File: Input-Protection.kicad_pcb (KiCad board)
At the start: 2 copper layers, 80 x 40 mm, 58 parts, among them J101 KLDX-0202-B, J102 EBWA-02-B, J103 EBWA-02-B, J104 KLDX-0202-B, Q201 MCU18P10Y-TP, Q601 BC846, Q602 MCU18P10Y-TP, U401 LM4040N-5.0, U501 AZV3002S-13

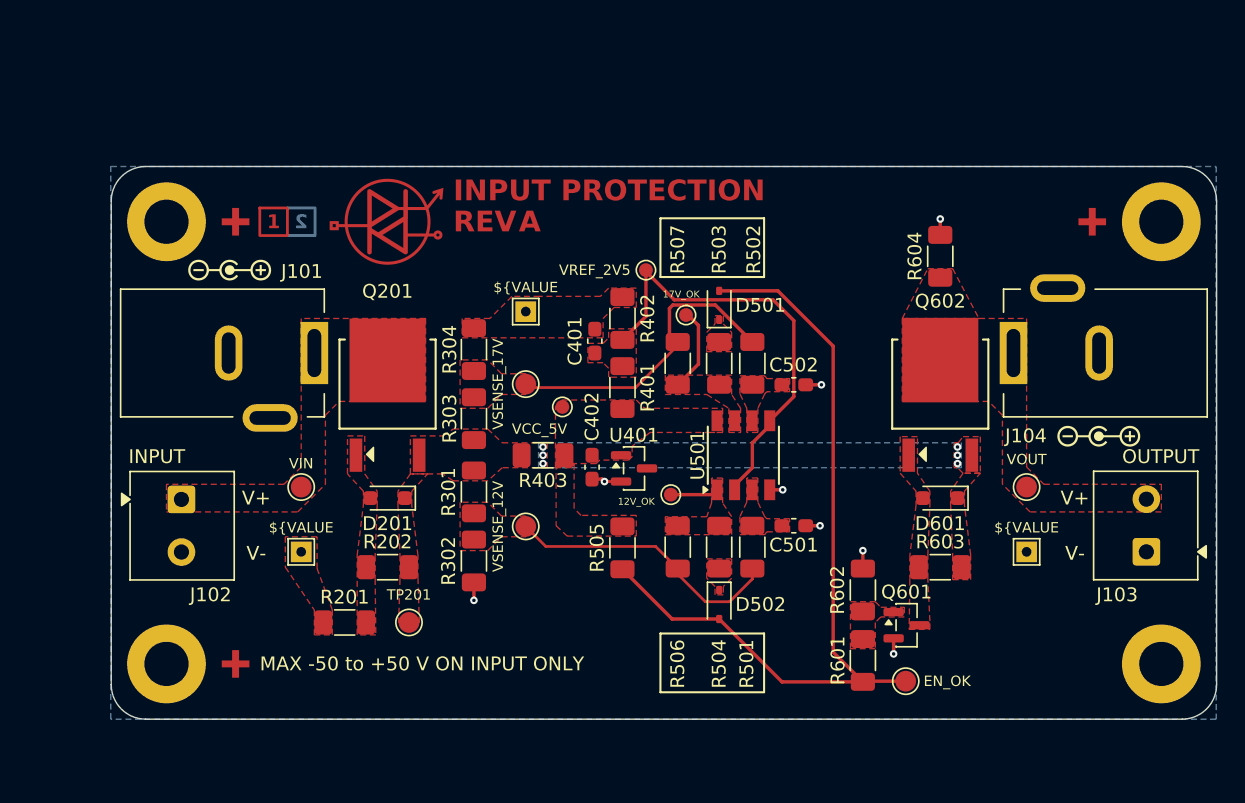
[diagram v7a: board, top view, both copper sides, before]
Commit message: feat!: added OC protection, redesigned board from near scratch, size increase
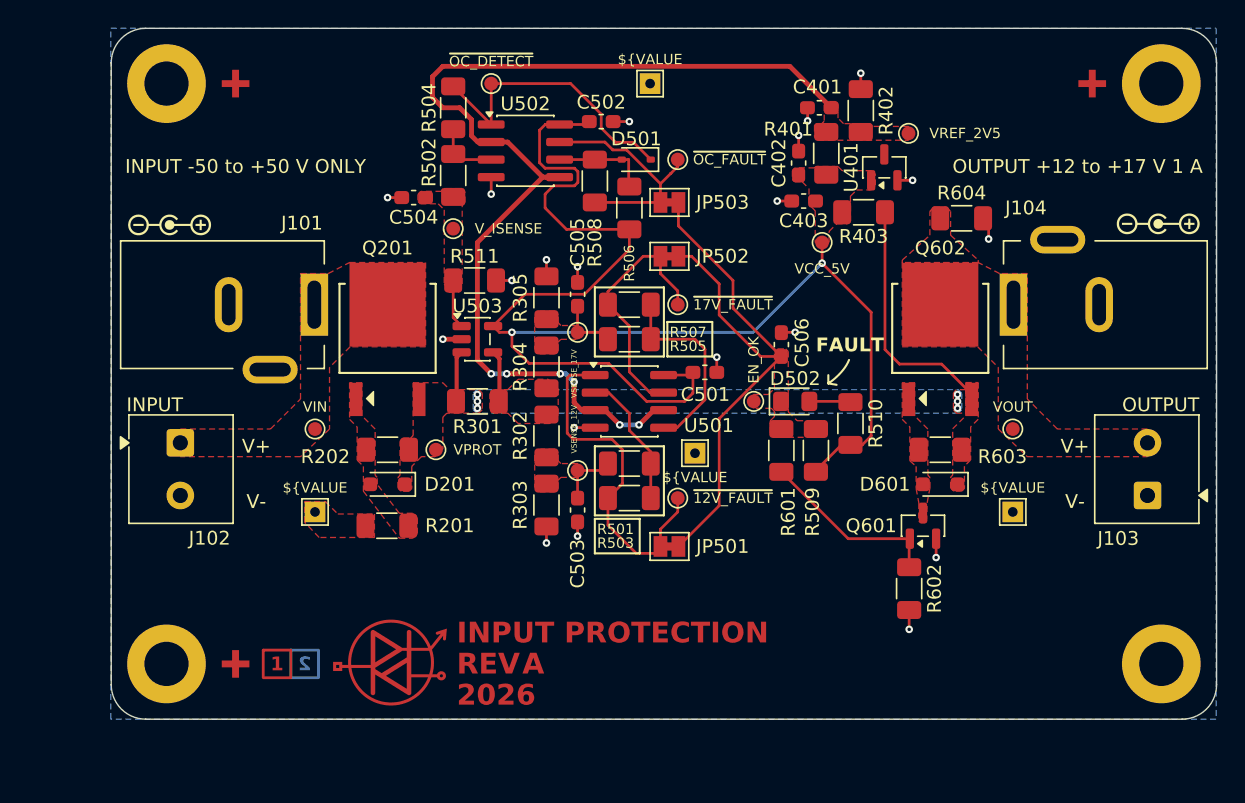
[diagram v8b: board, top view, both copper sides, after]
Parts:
- removed TP403: VCC_5V, RD-Testpoints:TestPoint_Pad_D1.0mm
- added C403: 100n, Capacitor_SMD:C_0603_1608Metric_Pad1.08x0.95mm_HandSolder, F.Cu at (167.7, 64.2)
- added C503: 10n, Capacitor_SMD:C_0603_1608Metric_Pad1.08x0.95mm_HandSolder, F.Cu at (151.3, 86.5)
- added C504: 10n, Capacitor_SMD:C_0603_1608Metric_Pad1.08x0.95mm_HandSolder, F.Cu at (139.5, 63.9)
- added C505: 10n, Capacitor_SMD:C_0603_1608Metric_Pad1.08x0.95mm_HandSolder, F.Cu at (151.3, 70.9)
- added C506: 1u, Capacitor_SMD:C_0603_1608Metric_Pad1.08x0.95mm_HandSolder, F.Cu at (166.1, 74.5)
- added JP501: SolderJumper_2_Bridged, Jumper:SolderJumper-2_P1.3mm_Bridged_Pad1.0x1.5mm, F.Cu at (158.0, 89.2)
- added JP502: SolderJumper_2_Bridged, Jumper:SolderJumper-2_P1.3mm_Bridged_Pad1.0x1.5mm, F.Cu at (158.0, 68.2)
- added JP503: SolderJumper_2_Bridged, Jumper:SolderJumper-2_P1.3mm_Bridged_Pad1.0x1.5mm, F.Cu at (158.0, 64.2)
- added R305: 10k, Resistor_SMD:R_1206_3216Metric_Pad1.30x1.75mm_HandSolder, F.Cu at (149.1, 71.2)
- added R508: 10k, Resistor_SMD:R_1206_3216Metric_Pad1.30x1.75mm_HandSolder, F.Cu at (152.6, 62.7)
- added R509: 10k, Resistor_SMD:R_1206_3216Metric_Pad1.30x1.75mm_HandSolder, F.Cu at (168.6, 82.2)
- added R510: 3.32k, Resistor_SMD:R_1206_3216Metric_Pad1.30x1.75mm_HandSolder, F.Cu at (171.1, 80.3)
- added R511: 22.1k, Resistor_SMD:R_1206_3216Metric_Pad1.30x1.75mm_HandSolder, F.Cu at (143.9, 69.9)
- added TP402: VCC_5V, RD-Testpoints:TestPoint_Pad_D1.0mm, F.Cu at (169.0, 67.2)
- added TP504: ~{OC_FAULT}, RD-Testpoints:TestPoint_Pad_D1.0mm, F.Cu at (158.6, 61.1)
- added TP505: V_ISENSE, RD-Testpoints:TestPoint_Pad_D1.0mm, F.Cu at (142.3, 66.2)
- added TP506: EN_OK, RD-Testpoints:TestPoint_Pad_D1.0mm, F.Cu at (164.1, 78.7)
- added TP507: GND, RD-Testpoints:TestPoint_THTPad_1.5x1.5mm_Drill0.7mm, F.Cu at (156.6, 55.6)
- added U502: LM393, Package_SO:SOIC-8_3.9x4.9mm_P1.27mm, F.Cu at (147.5, 60.5)
- added U503: INA169NA/3K, Package_TO_SOT_SMD:SOT-23-5, F.Cu at (144.1, 74.2)
- C402: value 100n -> 1u
- C501, C502: value 10n -> 100n
- D502: value 1N4148WS -> LED; footprint Diode_SMD:D_SOD-323 -> LED_SMD:LED_0805_2012Metric_Pad1.15x1.40mm_HandSolder
- R301: value 39.2k -> 100m
- R302: value 10k -> 39.2k
- R303: value 56.2k -> 10k
- R304: value 10k -> 56.2k
- R403: value 10k -> 3.32k
- R503, R504: value 470 -> 1M
- R505: value 47k -> 1k
- R506: value 1M -> 100k
- TP102, TP103, TP201, TP302, TP303: footprint RD-Testpoints:TestPoint_Pad_D1.5mm -> RD-Testpoints:TestPoint_Pad_D1.0mm
- TP501: value 12V_OK -> ~{12V_FAULT}
- TP502: value 17V_OK -> ~{OC_DETECT}
- TP503: value EN_OK -> ~{17V_FAULT}; footprint RD-Testpoints:TestPoint_Pad_D1.5mm -> RD-Testpoints:TestPoint_Pad_D1.0mm
- U501: value AZV3002S-13 -> LM393; footprint AZV3002S-13:Diodes_SO-8EP -> Package_SO:SOIC-8_3.9x4.9mm_P1.27mm
- moved R504 37.2 mm to (142.3, 57.4)
- moved ID901 32.0 mm to (130.6, 97.7)
- moved TP503 31.9 mm to (158.6, 71.7)
- moved R403 29.1 mm to (172.0, 65.0), turned to 0 degrees
- moved U401 28.3 mm to (173.5, 61.7), turned to 90 degrees
- moved C402 26.6 mm to (167.3, 61.4), turned to 90 degrees
- moved R502 25.6 mm to (142.3, 62.3)
- moved R506 24.8 mm to (155.1, 64.7), turned to -90 degrees
- moved C502 23.6 mm to (153.0, 58.4)
- moved C401 23.4 mm to (168.8, 57.4), turned to 180 degrees
- moved R402 22.9 mm to (171.8, 57.6)
- moved R401 22.5 mm to (169.3, 60.7)
- moved TP502 21.9 mm to (145.1, 55.6)
- moved TP401 21.4 mm to (175.3, 59.2), turned to 90 degrees
- moved R601 16.3 mm to (166.1, 82.2), turned to 90 degrees
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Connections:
- C501 pad 1: Net-(U501A-+) -> VCC_5V
- C502 pad 1: Net-(U501B--) -> VCC_5V
- D501 pad 1: Net-(D501-K) -> /ARCHITECTURE/5. COMPARATOR/~{OC_DETECT}
- D501 pad 2: /ARCHITECTURE/5. COMPARATOR/EN_OK -> /ARCHITECTURE/5. COMPARATOR/LATCH_IN
- D502 pad 1: Net-(D502-K) -> /ARCHITECTURE/5. COMPARATOR/EN_OK
- D502 pad 2: /ARCHITECTURE/5. COMPARATOR/EN_OK -> Net-(D502-A)
- R301 pad 1: /ARCHITECTURE/3. SENSING/VSENSE_12V -> /ARCHITECTURE/3. SENSING/ISENSE_N
- R302 pad 1: GND -> /ARCHITECTURE/3. SENSING/VSENSE_12V
- R302 pad 2: /ARCHITECTURE/3. SENSING/VSENSE_12V -> /ARCHITECTURE/3. SENSING/ISENSE_N
- R303 pad 1: /ARCHITECTURE/3. SENSING/VSENSE_17V -> GND
- R303 pad 2: /ARCHITECTURE/2. POLARITY PROTECTION/VPROT -> /ARCHITECTURE/3. SENSING/VSENSE_12V
- R304 pad 1: GND -> /ARCHITECTURE/3. SENSING/VSENSE_17V
- R304 pad 2: /ARCHITECTURE/3. SENSING/VSENSE_17V -> /ARCHITECTURE/3. SENSING/ISENSE_N
- R501 pad 1: Net-(U501A-+) -> Net-(U501A--)
- R502 pad 1: Net-(U501B--) -> /ARCHITECTURE/5. COMPARATOR/V_ISENSE
- R502 pad 2: /ARCHITECTURE/3. SENSING/VSENSE_17V -> Net-(U502A-+)
- R503 pad 1: Net-(D501-K) -> Net-(U501A--)
- R503 pad 2: /ARCHITECTURE/5. COMPARATOR/17V_OK -> /ARCHITECTURE/5. COMPARATOR/~{12V_FAULT}
- R504 pad 1: Net-(D502-K) -> Net-(U502A-+)
- R504 pad 2: /ARCHITECTURE/5. COMPARATOR/12V_OK -> /ARCHITECTURE/5. COMPARATOR/~{OC_DETECT}
- R505 pad 1: /ARCHITECTURE/5. COMPARATOR/EN_OK -> /ARCHITECTURE/3. SENSING/VSENSE_17V
- R505 pad 2: VCC_5V -> Net-(U501B-+)
- R506 pad 1: /ARCHITECTURE/3. SENSING/VSENSE_12V -> /ARCHITECTURE/5. COMPARATOR/LATCH_IN
- R506 pad 2: /ARCHITECTURE/5. COMPARATOR/12V_OK -> VCC_5V
- R507 pad 1: /ARCHITECTURE/3. SENSING/VSENSE_17V -> Net-(U501B-+)
- R507 pad 2: /ARCHITECTURE/5. COMPARATOR/17V_OK -> /ARCHITECTURE/5. COMPARATOR/~{17V_FAULT}
- TP501 pad 1: /ARCHITECTURE/5. COMPARATOR/12V_OK -> /ARCHITECTURE/5. COMPARATOR/~{12V_FAULT}
- TP502 pad 1: /ARCHITECTURE/5. COMPARATOR/17V_OK -> /ARCHITECTURE/5. COMPARATOR/~{OC_DETECT}
- TP503 pad 1: /ARCHITECTURE/5. COMPARATOR/EN_OK -> /ARCHITECTURE/5. COMPARATOR/~{17V_FAULT}
- U501 pad 1: /ARCHITECTURE/5. COMPARATOR/12V_OK -> /ARCHITECTURE/5. COMPARATOR/~{12V_FAULT}
- U501 pad 2: VREF_2V5 -> Net-(U501A--)
- U501 pad 3: Net-(U501A-+) -> VREF_2V5
- U501 pad 5: VREF_2V5 -> Net-(U501B-+)
- U501 pad 6: Net-(U501B--) -> VREF_2V5
- U501 pad 7: /ARCHITECTURE/5. COMPARATOR/17V_OK -> /ARCHITECTURE/5. COMPARATOR/~{17V_FAULT}
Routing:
- net VCC_5V: track 0.00 -> 100.6 mm, vias 0 -> 2
- net VREF_2V5: track 31.8 -> 76.1 mm, vias 0 -> 6
- net /ARCHITECTURE/5. COMPARATOR/~{12V_FAULT}: track 0.00 -> 25.7 mm
- net /ARCHITECTURE/2. POLARITY PROTECTION/VPROT: track 0.00 -> 21.6 mm
- net /ARCHITECTURE/5. COMPARATOR/~{OC_DETECT}: track 0.00 -> 21.3 mm
- net /ARCHITECTURE/5. COMPARATOR/~{17V_FAULT}: track 0.00 -> 18.4 mm
- net /ARCHITECTURE/3. SENSING/VSENSE_17V: track 22.6 -> 4.29 mm
- net /ARCHITECTURE/5. COMPARATOR/~{OC_FAULT}: track 0.00 -> 17.1 mm
- net /ARCHITECTURE/5. COMPARATOR/EN_OK: track 59.5 -> 42.9 mm
- net /ARCHITECTURE/3. SENSING/VSENSE_12V: track 20.3 -> 4.41 mm
- net Net-(U501B-+): track 0.00 -> 14.2 mm
- net GND: track 10.2 -> 24.0 mm, vias 8 -> 20
- net Net-(Q601-B): track 0.00 -> 13.4 mm
- net Net-(U501A--): track 0.00 -> 10.1 mm
- net /ARCHITECTURE/5. COMPARATOR/LATCH_IN: track 0.00 -> 6.47 mm
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- added copper zone on F.Cu, net /ARCHITECTURE/3. SENSING/ISENSE_N
- added copper zone on F.Cu, net /ARCHITECTURE/5. COMPARATOR/EN_OK
- added copper zone on F.Cu, net /ARCHITECTURE/5. COMPARATOR/V_ISENSE
- removed copper zone on F.Cu, net /ARCHITECTURE/5. COMPARATOR/12V_OK
- removed copper zone on F.Cu, net /ARCHITECTURE/5. COMPARATOR/17V_OK
- removed copper zone on F.Cu, net Net-(D501-K)
- removed copper zone on F.Cu, net Net-(D502-K)
- removed copper zone on F.Cu, net Net-(Q601-B)
- removed copper zone on F.Cu, net Net-(U501A-+)
- removed copper zone on F.Cu, net Net-(U501B--)
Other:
- board size 80 x 40 mm -> 80 x 50 mm
- board text added: "2026"
- board text added: "FAULT"
- board text added: "INPUT -50 to +50 V ONLY"
- board text added: "OUTPUT +12 to +17 V 1 A"
- board text removed: "MAX -50 to +50 V ON INPUT ONLY"
